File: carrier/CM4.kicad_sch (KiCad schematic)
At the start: 33 parts, among them J1 AudioJack3_Switch, J2 52271-0879, J3 Micro_SD_Card, Q1 2N2219, SW1 SW_Push, U1 AP22814AW5

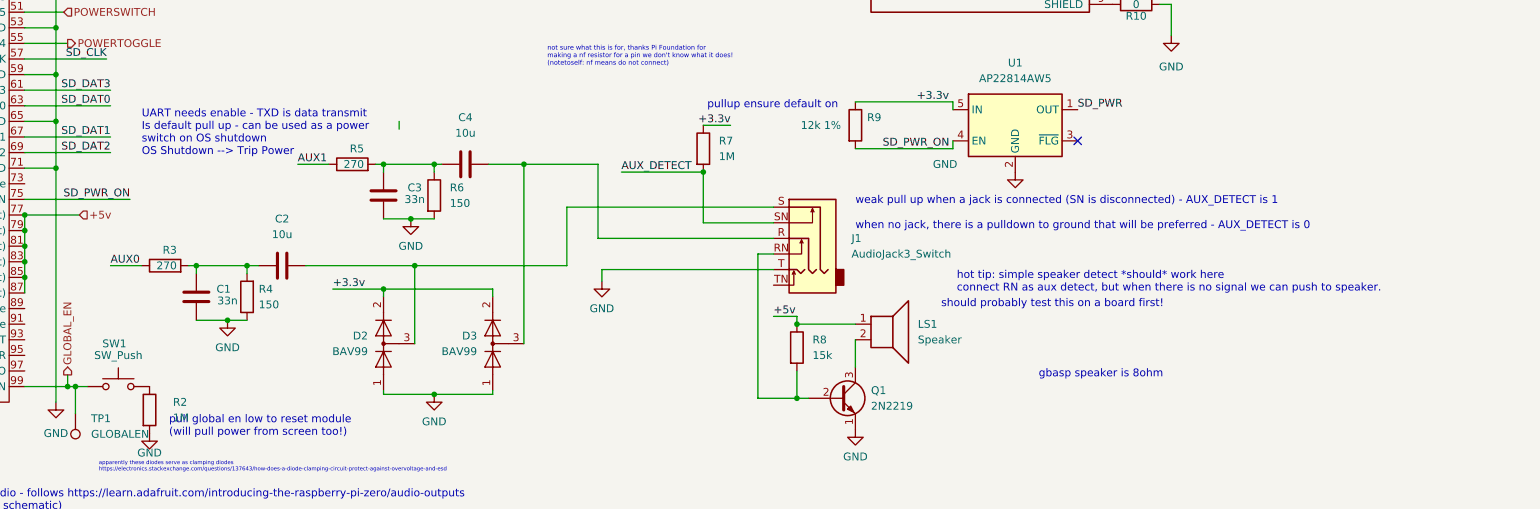
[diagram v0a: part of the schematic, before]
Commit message: need to finish footprint assignments then can do rev2 pcb (cooler one)
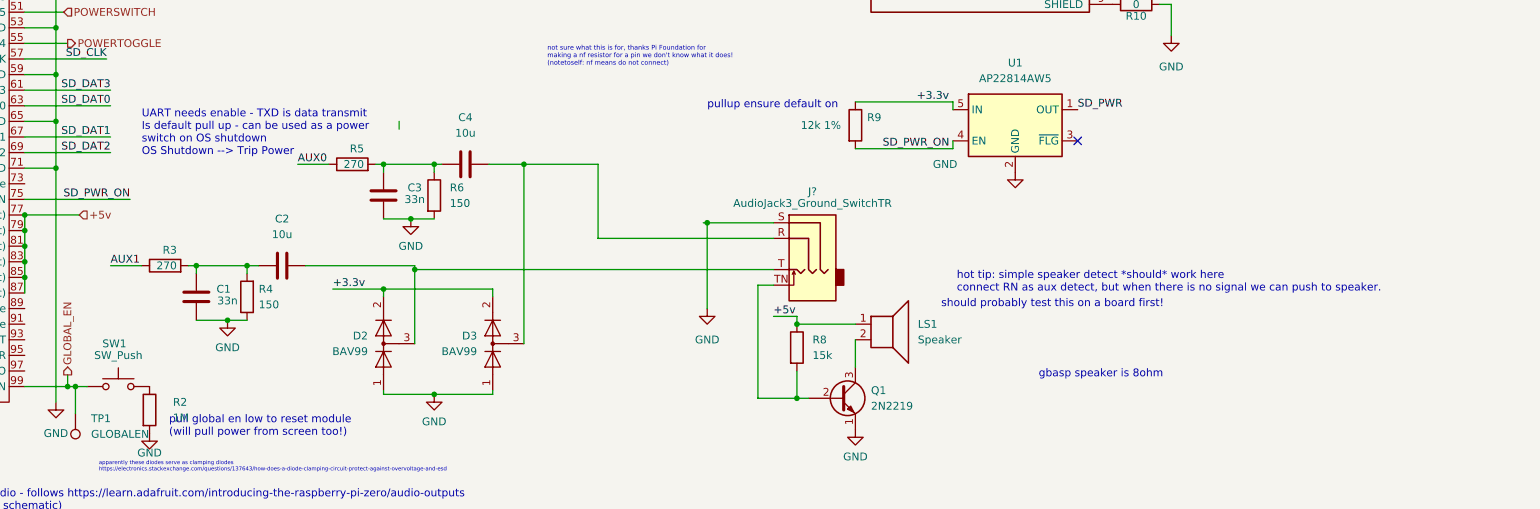
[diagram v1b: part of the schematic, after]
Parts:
- removed J1: AudioJack3_Switch, audio:audio, symbol Connector:AudioJack3_Switch
- removed R7: 1M, symbol Device:R
- added J?: AudioJack3_Ground_SwitchTR, audio:CUI-SJ-43515TS-SMT-TR-0, symbol Connector:AudioJack3_Ground_SwitchTR
- J3: footprint sdcard:HRS_DM3CS-SF -> sdcard:GCT_MEM2067-02-180-00-A_REVB
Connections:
- net AUX0: now also R5.1; no longer R3.1
- net AUX1: now also R3.1; no longer R5.1
- net GND: now also J?.S
- net at C2.2, D2.3 (K): now also J?.T
- net at C4.2, D3.3 (K): now also J?.R
- net at Q1.2 (B), R8.2: now also J?.TN
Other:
- note removed: "weak pull up when a jack is connected (SN is disconnected) - AUX_DETECT is 1 when no jack, there is a pulldown to ground that will be preferred - AUX_DETECT is 0"

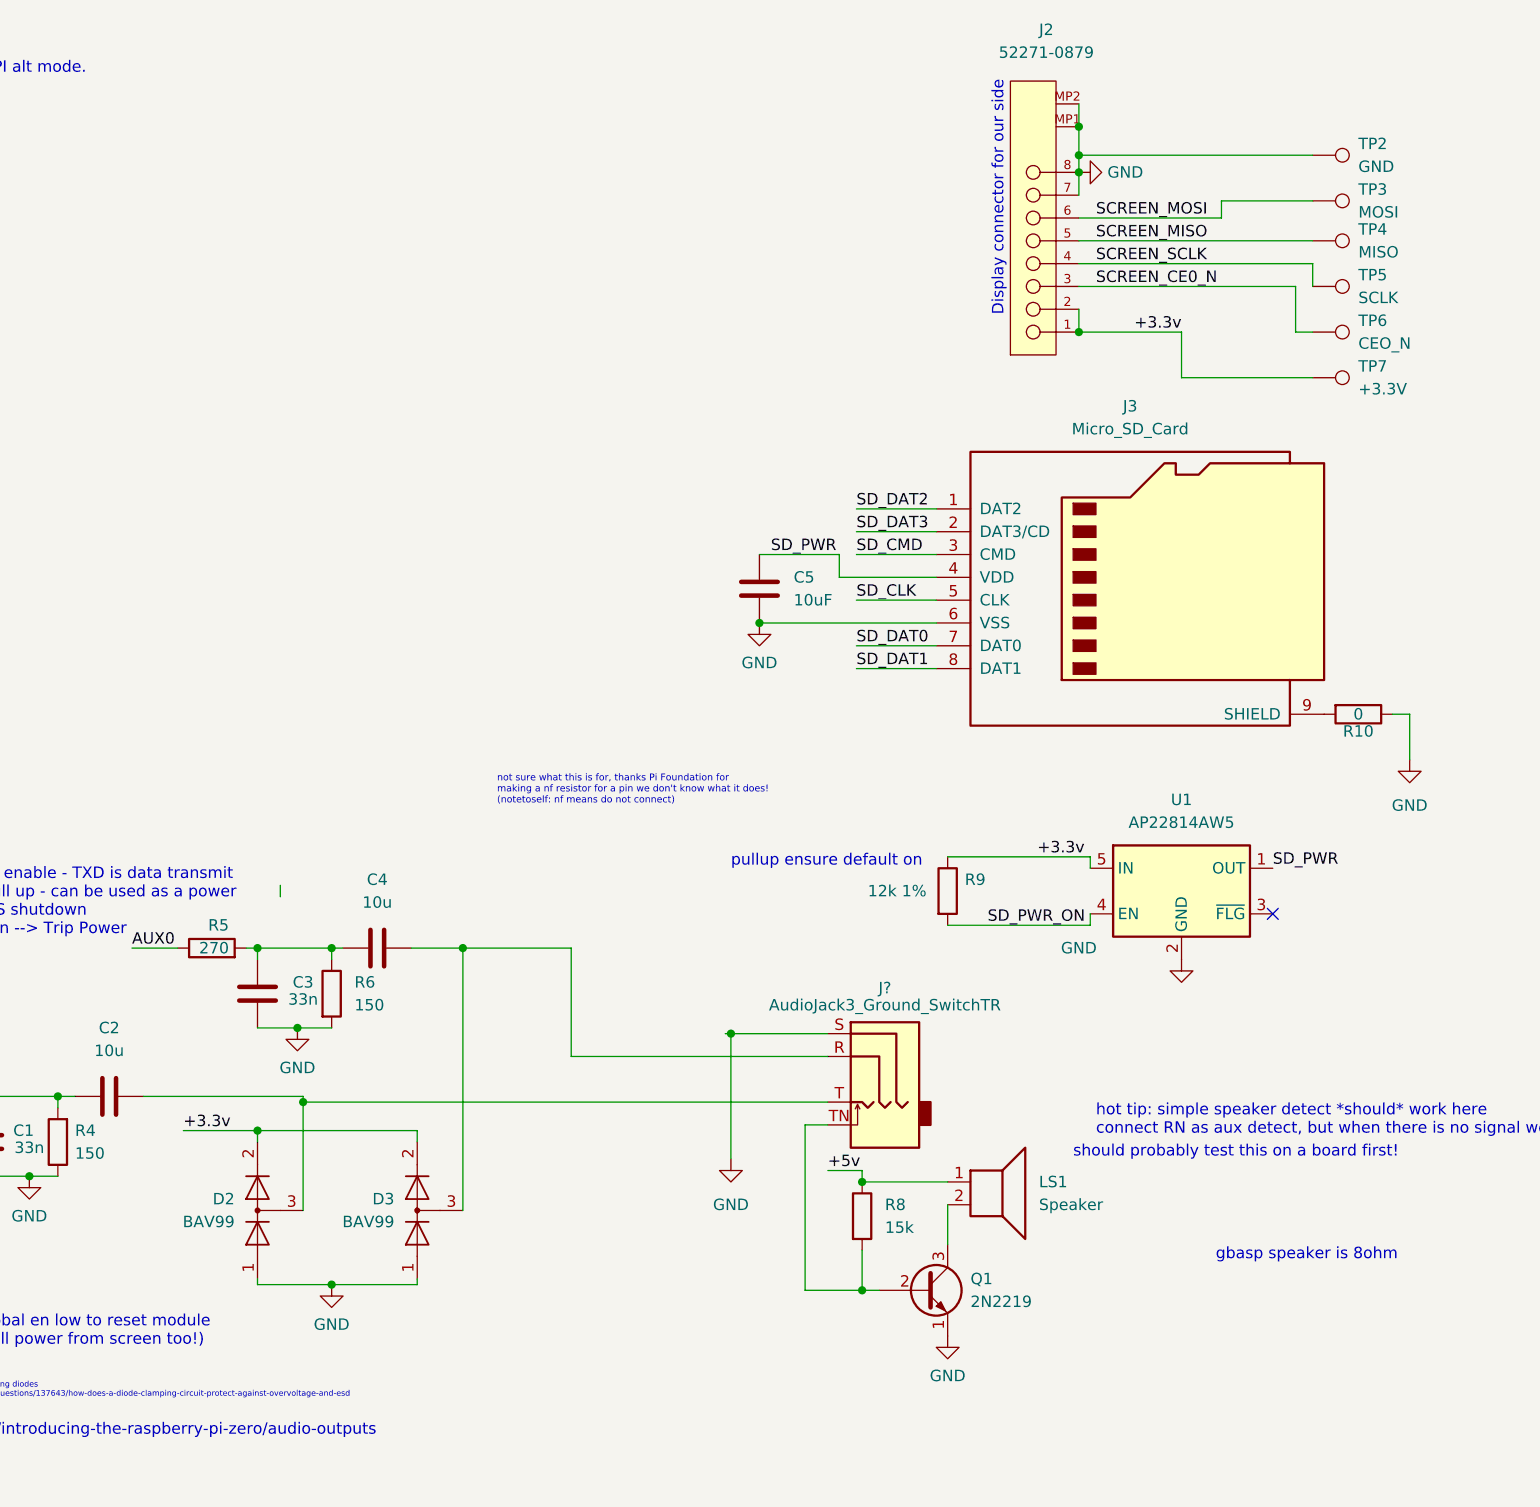
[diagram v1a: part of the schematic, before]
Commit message: new footprints - order stuff soon
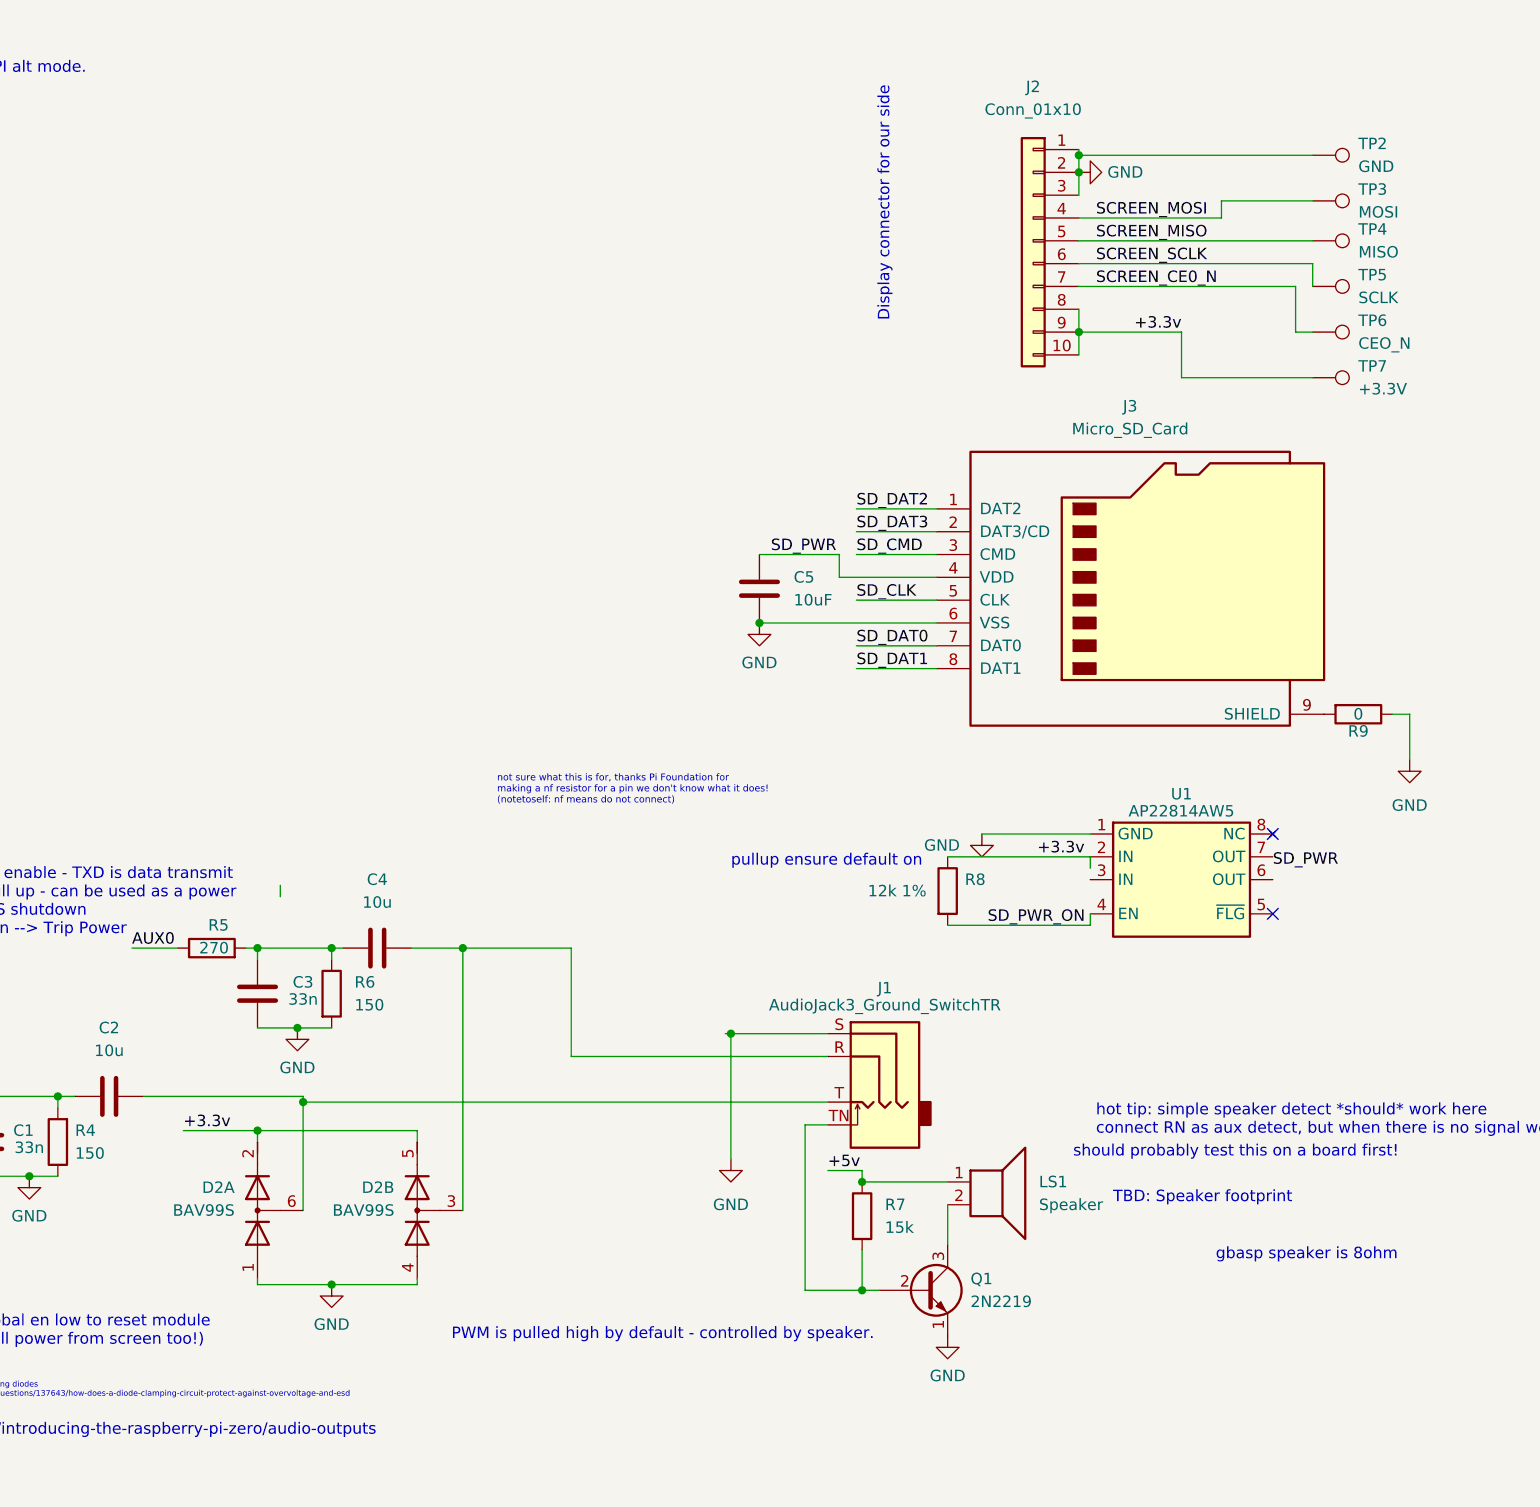
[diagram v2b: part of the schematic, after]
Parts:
- removed D2, D3: BAV99, Package_TO_SOT_SMD:SOT-23, symbol Diode:BAV99
- removed J2: 52271-0879, MOLEXZIF:Molex-52271-0879-Manufacturer_Recommended, symbol MOLEXZIF:52271-0879
- added D2: BAV99S, Package_TO_SOT_SMD:SOT-363_SC-70-6, symbol Diode:BAV99S
- added J2: Conn_01x10, CM4IO:522711169, symbol Connector_Generic:Conn_01x10
- D1: footprint LED_SMD:LED_0805_2012Metric_Pad1.15x1.40mm_HandSolder -> LED_SMD:LED_0603_1608Metric_Pad1.05x0.95mm_HandSolder
- LS1: footprint (none) -> CM4IO:speaker
- R1: footprint Resistor_SMD:R_0402_1005Metric_Pad0.72x0.64mm_HandSolder -> Resistor_SMD:R_0603_1608Metric_Pad0.98x0.95mm_HandSolder
- R2: footprint (none) -> Resistor_SMD:R_0603_1608Metric_Pad0.98x0.95mm_HandSolder
- R7: renamed from R8; footprint (none) -> Resistor_SMD:R_0603_1608Metric_Pad0.98x0.95mm_HandSolder
- R8: renamed from R9; footprint Resistor_SMD:R_0402_1005Metric_Pad0.72x0.64mm_HandSolder -> Resistor_SMD:R_0603_1608Metric_Pad0.98x0.95mm_HandSolder
- SW1: footprint (none) -> Button_Switch_THT:SW_PUSH_6mm_H4.3mm
- TP1: footprint (none) -> TestPoint:TestPoint_Pad_2.0x2.0mm
- TP2, TP3, TP4, TP5, TP6, TP7: footprint TestPoint:TestPoint_Pad_1.0x1.0mm -> TestPoint:TestPoint_Pad_2.0x2.0mm
- U1: footprint Package_TO_SOT_SMD:SOT-23-5 -> Package_SO:MSOP-8-1EP_3x3mm_P0.65mm_EP1.68x1.88mm
- gave numbers to parts that had none: 1
- renumbered R10 to R9
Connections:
- net +3.3v: now also U1.2 (IN), D2.2 (K2), D2.5 (K4), J2.10 (Pin_10), J2.8 (Pin_8), J2.9 (Pin_9); no longer U1.5 (IN)
- net GND: now also U1.1 (GND), D2.1 (A1), D2.4 (A3), J2.1 (Pin_1), J2.2 (Pin_2), J2.3 (Pin_3); no longer U1.2 (GND)
- net SCREEN_CE0_N: now also J2.7 (Pin_7)
- net SCREEN_MISO: now also J2.5 (Pin_5)
- net SCREEN_MOSI: now also J2.4 (Pin_4)
- net SCREEN_SCLK: now also J2.6 (Pin_6)
- net SD_PWR: no longer U1.1 (OUT)
- net at C2.2, J1.T: now also D2.6 (K3A4)
- net at C4.2, J1.R: now also D2.3 (K1A2)
- no-connect marks 1 -> 2
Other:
- note added: "PWM is pulled high by default - controlled by speaker."
- note added: "TBD: Speaker footprint"

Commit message: buggy
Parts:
- added unit 2 of Module1
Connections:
- net +5v: no longer Module1.79 (+5v_(Input)), Module1.81 (+5v_(Input)), Module1.83 (+5v_(Input)), Module1.85 (+5v_(Input)), Module1.87 (+5v_(Input))
- new net: Module1.85 (+5v_(Input)), Module1.87 (+5v_(Input))

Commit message: go back to tomrw
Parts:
- removed unit 2 of Module1
